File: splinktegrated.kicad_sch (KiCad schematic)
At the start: 62 parts, among them J1 USB_C_Receptacle_USB2.0, J10 NA_Ribbon, J11 NA_Serial, J12 NA_Conn_01x04_Female, J13 Conn_01x01_Socket, J14 Cirque, J15 Conn_01x01_Socket, J16 Conn_01x01_Socket, J17 Conn_01x01_Socket, J2 NA_Conn_01x04_Female, J3 NA_Conn_01x04_Female, J4 NA_Conn_01x04_Female, J5 Conn_01x02, J6 Cirque, J7 NA_trackball, J8 NA_Ribbon, J9 NA_RGB, SW1 NA_SW_SPST, SW2 NA_SW_SPST, U1 RP2040, U2 USBLC6-2P6, U3 XC6210B332MR-G, U4 USBLC6-2P6, U5 W25Q128JVS, Y1 Crystal_GND24

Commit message: add pin
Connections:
- net ss_l: now also J6.3 (Pin_3)
- net SPI_CS: no longer names the net of U1.29 (GPIO18)
- net SPI_CS: no longer J6.3 (Pin_3)
- no-connect marks 14 -> 15
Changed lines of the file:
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@@
 	)
 	(no_connect
+		(at 182.88 104.14)
+	)
+	(no_connect
 		(at 431.8 64.77)
 	)
@@
 	(global_label "ss_l"
 		(shape input)
+		(at 431.8 57.15 180)
+		(effects
+			(font
+				(size 1.27 1.27)
+			)
+			(justify right)
+		)
+		(property "Intersheetrefs" "${INTERSHEET_REFS}"
+			(at 427.3307 57.0706 0)
+			(effects
+				(font
+					(size 1.27 1.27)
+				)
+				(justify right)
+				(hide yes)
+			)
+		)
+	)
+	(global_label "ss_l"
+		(shape input)
 		(at 312.42 25.4 180)
 		(effects
@@
 		)
 	)
-	(global_label "SPI_CS"
-		(shape input)
-		(at 431.8 57.15 180)
-		(effects
-			(font
-				(size 1.27 1.27)
-			)
-			(justify right)
-		)
-		(property "Intersheetrefs" "${INTERSHEET_REFS}"
-			(at 402.59 17.78 0)
-			(effects
-				(font
-					(size 1.27 1.27)
-				)
-				(hide yes)
-			)
-		)
-	)
 	(global_label "col4_l"
 		(shape input)
@@
 				(hide yes)
 			)
-		)
-	)
-	(global_label "SPI_CS"
-		(shape input)
-		(at 182.88 104.14 0)
-		(effects
-			(font
-				(size 1.27 1.27)
-			)
-			(justify left)
-		)
-		(property "Intersheetrefs" "${INTERSHEET_REFS}"
-			(at 212.09 143.51 0)
-			(effects
-				(font
-					(size 1.27 1.27)
-				)
-				(hide yes)
-			)

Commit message: add hands jumper
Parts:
- added NA_JP6, NA_JP7: NA_Jumper_2_Open, local-libraries:SolderJumper-2_P1.3mm_Open_TrianglePad1.0x1.5mm, symbol Jumper:Jumper_2_Open
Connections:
- net +3V3: now also NA_JP7.2 (B)
- net GND: now also NA_JP6.2 (B)
- net hand: now reaches U1.18 (GPIO15)
- net hand: now also NA_JP6.1 (A), NA_JP7.1 (A)
- no-connect marks 15 -> 14
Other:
- note added: "Hand"

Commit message: handedness resistor
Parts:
- added R12: 5.1k, Resistor_SMD:R_0402_1005Metric, symbol Device:R
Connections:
- net hand: now also R12.2; no longer NA_JP6.1 (A), NA_JP7.1 (A)
- new net: NA_JP6.1 (A), NA_JP7.1 (A), R12.1
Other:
- moved on the sheet: NA_JP6, NA_JP7
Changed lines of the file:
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@@
 	)
 	(junction
-		(at 422.91 128.27)
-		(diameter 0)
-		(color 0 0 0 0)
-	)
-	(junction
 		(at 111.76 96.52)
 		(diameter 0)
@@
 	)
 	(junction
+		(at 431.8 128.27)
+		(diameter 0)
+		(color 0 0 0 0)
+	)
+	(junction
 		(at 243.84 119.38)
 		(diameter 0)
@@
 	(wire
 		(pts
-			(xy 422.91 124.46) (xy 422.91 128.27)
-		)
-		(stroke
-			(width 0)
-			(type default)
-		)
-	)
-	(wire
-		(pts
 			(xy 33.02 115.57) (xy 33.02 118.11)
 		)
@@
 	(wire
 		(pts
-			(xy 422.91 128.27) (xy 422.91 132.08)
+			(xy 431.8 124.46) (xy 431.8 128.27)
 		)
 		(stroke
@@
 	(wire
 		(pts
+			(xy 431.8 128.27) (xy 431.8 132.08)
+		)
+		(stroke
+			(width 0)
+			(type default)
+		)
+	)
+	(wire
+		(pts
 			(xy 182.88 86.36) (xy 191.77 86.36)
 		)
@@
 	(wire
 		(pts
-			(xy 425.45 124.46) (xy 422.91 124.46)
+			(xy 434.34 124.46) (xy 431.8 124.46)
 		)
 		(stroke
@@
 	(wire
 		(pts
+			(xy 430.53 128.27) (xy 431.8 128.27)
+		)
+		(stroke
+			(width 0)
+			(type default)
+		)
+	)
+	(wire
+		(pts
 			(xy 97.79 105.41) (xy 97.79 106.68)
 		)
@@
 	(wire
 		(pts
-			(xy 425.45 132.08) (xy 422.91 132.08)
+			(xy 434.34 132.08) (xy 431.8 132.08)
 		)
 		(stroke
@@
 	(symbol
 		(lib_id "Jumper:Jumper_2_Open")
-		(at 430.53 132.08 0)
+		(at 439.42 132.08 0)
 		(unit 1)
 		(exclude_from_sim no)
@@
 		(dnp no)
 		(property "Reference" "NA_JP7"
-			(at 429.514 128.778 0)
+			(at 438.404 128.778 0)
 			(effects
 				(font
@@
 		)
 		(property "Value" "NA_Jumper_2_Open"
-			(at 444.246 126.238 0)
+			(at 453.136 126.238 0)
 			(effects
 				(font
@@
 		)
 		(property "Footprint" "local-libraries:SolderJumper-2_P1.3mm_Open_TrianglePad1.0x1.5mm"
-			(at 430.53 132.08 0)
+			(at 439.42 132.08 0)
 			(effects
 				(font
@@
 		)
 		(property "Datasheet" "~"
-			(at 430.53 132.08 0)
+			(at 439.42 132.08 0)
 			(effects
 				(font
@@
 		)
 		(property "Description" ""
-			(at 430.53 132.08 0)
+			(at 439.42 132.08 0)
 			(effects
 				(font
@@
 	(symbol
 		(lib_id "Jumper:Jumper_2_Open")
-		(at 430.53 124.46 0)
+		(at 439.42 124.46 0)
 		(unit 1)
 		(exclude_from_sim no)
@@
 		(dnp no)
 		(property "Reference" "NA_JP6"
-			(at 429.514 121.158 0)
+			(at 438.404 121.158 0)
 			(effects
 				(font
@@
 		)
 		(property "Value" "NA_Jumper_2_Open"
-			(at 444.246 118.618 0)
+			(at 453.136 118.618 0)
 			(effects
 				(font
@@
 		)
 		(property "Footprint" "local-libraries:SolderJumper-2_P1.3mm_Open_TrianglePad1.0x1.5mm"
-			(at 430.53 124.46 0)
+			(at 439.42 124.46 0)
 			(effects
 				(font
@@
 		)
 		(property "Datasheet" "~"
-			(at 430.53 124.46 0)
+			(at 439.42 124.46 0)
 			(effects
 				(font
@@
 		)
 		(property "Description" ""
-			(at 430.53 124.46 0)
+			(at 439.42 124.46 0)
 			(effects
 				(font
@@
 	)
 	(symbol
+		(lib_id "Device:R")
+		(at 426.72 128.27 270)
+		(unit 1)
+		(exclude_from_sim no)
+		(in_bom yes)
+		(on_board yes)
+		(dnp no)
+		(property "Reference" "R12"
+			(at 426.72 130.81 90)
+			(effects
+				(font
+					(size 1.27 1.27)
+				)
+			)
+		)
+		(property "Value" "5.1k"
+			(at 426.72 128.27 90)
+			(effects
+				(font
+					(size 1.27 1.27)
+				)
+			)
+		)
+		(property "Footprint" "Resistor_SMD:R_0402_1005Metric"
+			(at 426.72 126.492 90)
+			(effects
+				(font
+					(size 1.27 1.27)
+				)
+				(hide yes)
+			)
+		)
+		(property "Datasheet" "~"
+			(at 426.72 128.27 0)
+			(effects
+				(font
+					(size 1.27 1.27)
+				)
+				(hide yes)
+			)
+		)
+		(property "Description" ""
+			(at 426.72 128.27 0)
+			(effects
+				(font
+					(size 1.27 1.27)
+				)
+				(hide yes)
+			)
+		)
+		(property "LCSC" "C25905"
+			(at 426.72 128.27 0)
+			(effects
+				(font
+					(size 1.27 1.27)
+				)
+				(hide yes)
+			)
+		)
+		(pin "1"
+		)
+		(pin "2"
+		)
+		(instances
+			(project "splinktegrated"
+				(path "/7353e96a-343a-4876-b497-b1d205a14d97"
+					(reference "R12")
+					(unit 1)
+				)
+			)
+		)
+	)
+	(symbol
 		(lib_id "Power_Protection:USBLC6-2P6")
 		(at -93.345 115.57 0)
@@
 	(symbol
 		(lib_id "power:GND")
-		(at 435.61 124.46 90)
+		(at 444.5 124.46 90)
 		(unit 1)
 		(exclude_from_sim no)
@@
 		(dnp no)
 		(property "Reference" "#PWR039"
-			(at 441.96 124.46 0)
+			(at 450.85 124.46 0)
 			(effects
 				(font
@@
 		)
 		(property "Value" "GND"
-			(at 443.8649 124.616 90)
+			(at 452.7549 124.616 90)
 			(effects
 				(font
@@
 		)
 		(property "Footprint" ""
-			(at 435.61 124.46 0)
+			(at 444.5 124.46 0)
 			(effects
 				(font
@@
 		)
 		(property "Datasheet" ""
-			(at 435.61 124.46 0)
+			(at 444.5 124.46 0)
 			(effects
 				(font
@@
 		)
 		(property "Description" ""
-			(at 435.61 124.46 0)
+			(at 444.5 124.46 0)
 			(effects
 				(font
@@
 	(symbol
 		(lib_id "power:+3.3V")
-		(at 435.61 132.08 270)
+		(at 444.5 132.08 270)
 		(unit 1)
 		(exclude_from_sim no)
@@
 		(dnp no)
 		(property "Reference" "#PWR040"
-			(at 431.8 132.08 0)
+			(at 440.69 132.08 0)
 			(effects
 				(font
@@
 		)
 		(property "Value" "+3V3"
-			(at 439.42 132.08 0)
+			(at 448.31 132.08 0)
 			(effects
 				(font
@@
 		)
 		(property "Footprint" ""
-			(at 435.61 132.08 0)
+			(at 444.5 132.08 0)
 			(effects
 				(font
@@
 		)
 		(property "Datasheet" ""
-			(at 435.61 132.08 0)
+			(at 444.5 132.08 0)
 			(effects
 				(font
@@
 		)
 		(property "Description" ""
-			(at 435.61 132.08 0)
+			(at 444.5 132.08 0)
 			(effects
 				(font

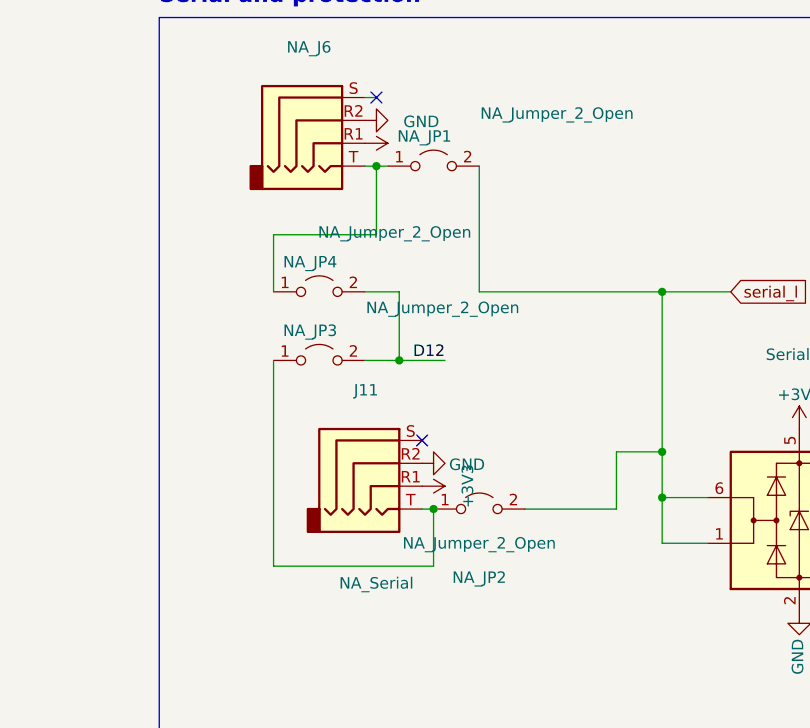
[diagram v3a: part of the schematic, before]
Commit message: remove full duplex jumper
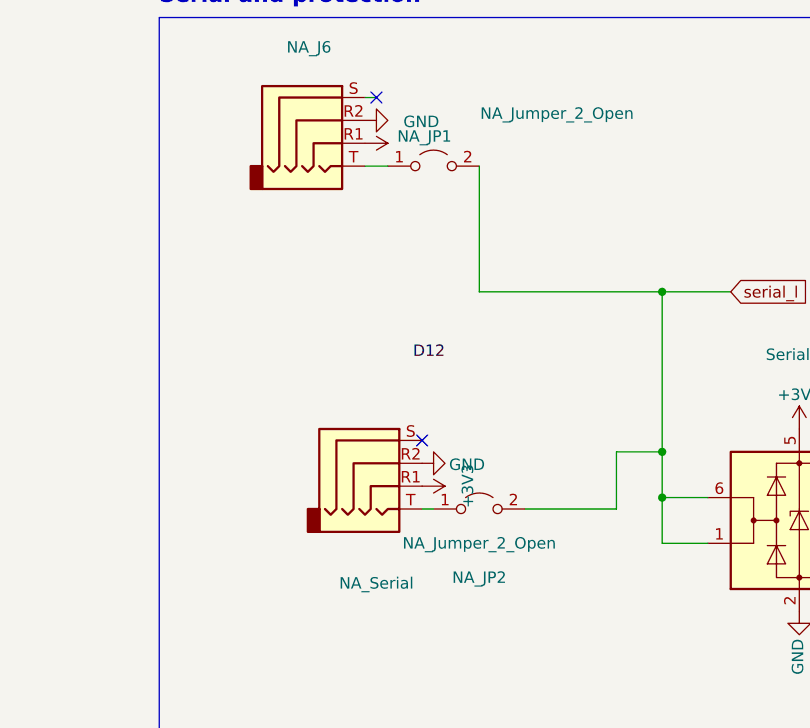
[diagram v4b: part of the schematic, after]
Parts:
- removed NA_JP3, NA_JP4: NA_Jumper_2_Open, local-libraries:SolderJumper-2_P1.3mm_Open_TrianglePad1.0x1.5mm, symbol Jumper:Jumper_2_Open

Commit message: additional hotplug protection
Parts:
- removed D2: B5817, Diode_SMD:D_SOD-323, symbol Device:D_Schottky
- added C15: 10u, Capacitor_SMD:C_1206_3216Metric, symbol Djinn-rescue:CP-Device
- added D3: SMF5.0CA, Diode_SMD:D_SOD-123, symbol Device:D_TVS
- added Q1: AO3401A, Package_TO_SOT_SMD:TSOT-23, symbol Transistor_FET:AO3401A
- added R13: 120, Resistor_SMD:R_0402_1005Metric, symbol Device:R
- added R14: 1.5k, Resistor_SMD:R_0402_1005Metric, symbol Device:R
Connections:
- net +3V3: now also R14.2
- net +5V: now also C15.1, Q1.3 (D)
- net GND: now also C15.2, D3.2 (A2), Q1.1 (G)
- net serial_l: now also R13.2, R14.1; no longer NA_JP1.2 (B), NA_JP2.2 (B), U2.1 (I/O1), U2.6 (I/O1)
- net at F1.2: now also D3.1 (A1), Q1.2 (S)
- new net: NA_JP1.2 (B), NA_JP2.2 (B), R13.1, U2.1 (I/O1), U2.6 (I/O1)
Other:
- moved on the sheet: F1, J12, J4
